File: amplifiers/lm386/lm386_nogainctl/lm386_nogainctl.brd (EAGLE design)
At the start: 55.5 x 35.3 mm, 12 parts, among them IC1 LM386N-4

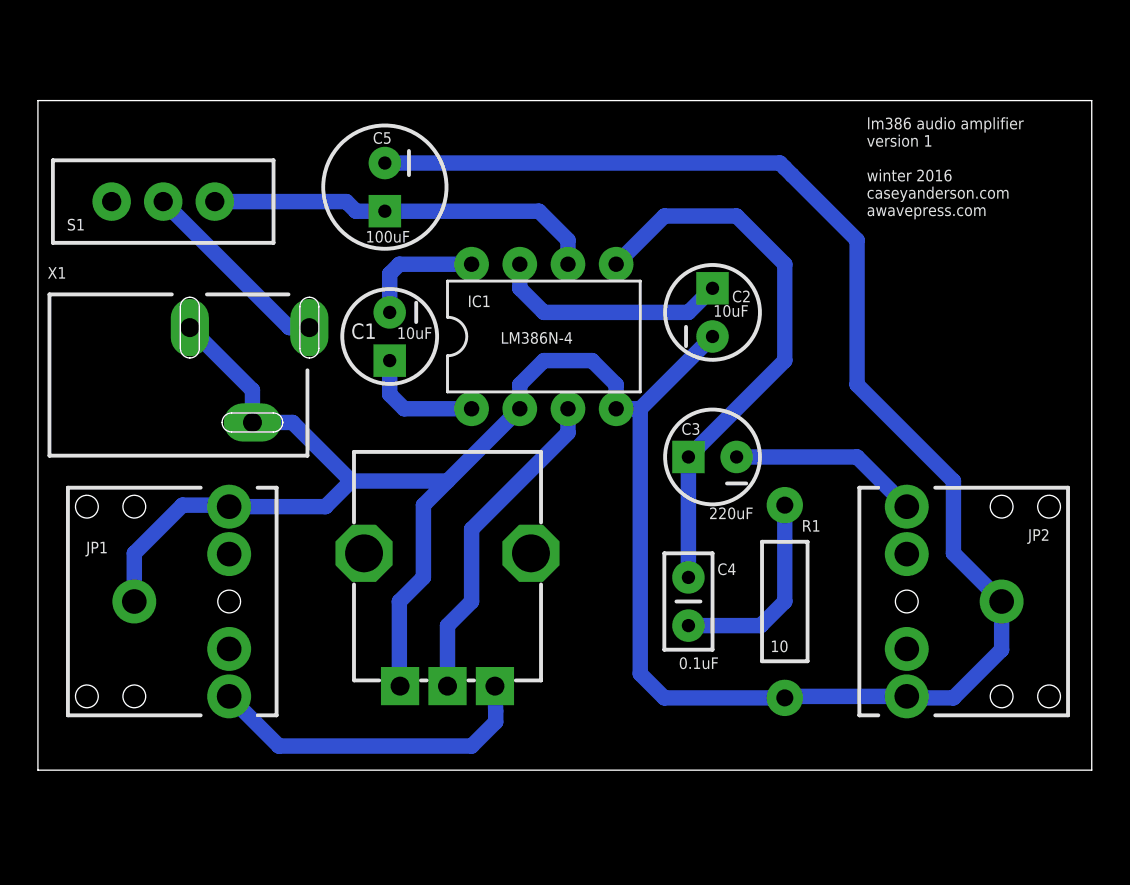
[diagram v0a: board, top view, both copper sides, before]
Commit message: updated to version 3, check on screw size and hole placement needed for confirmation
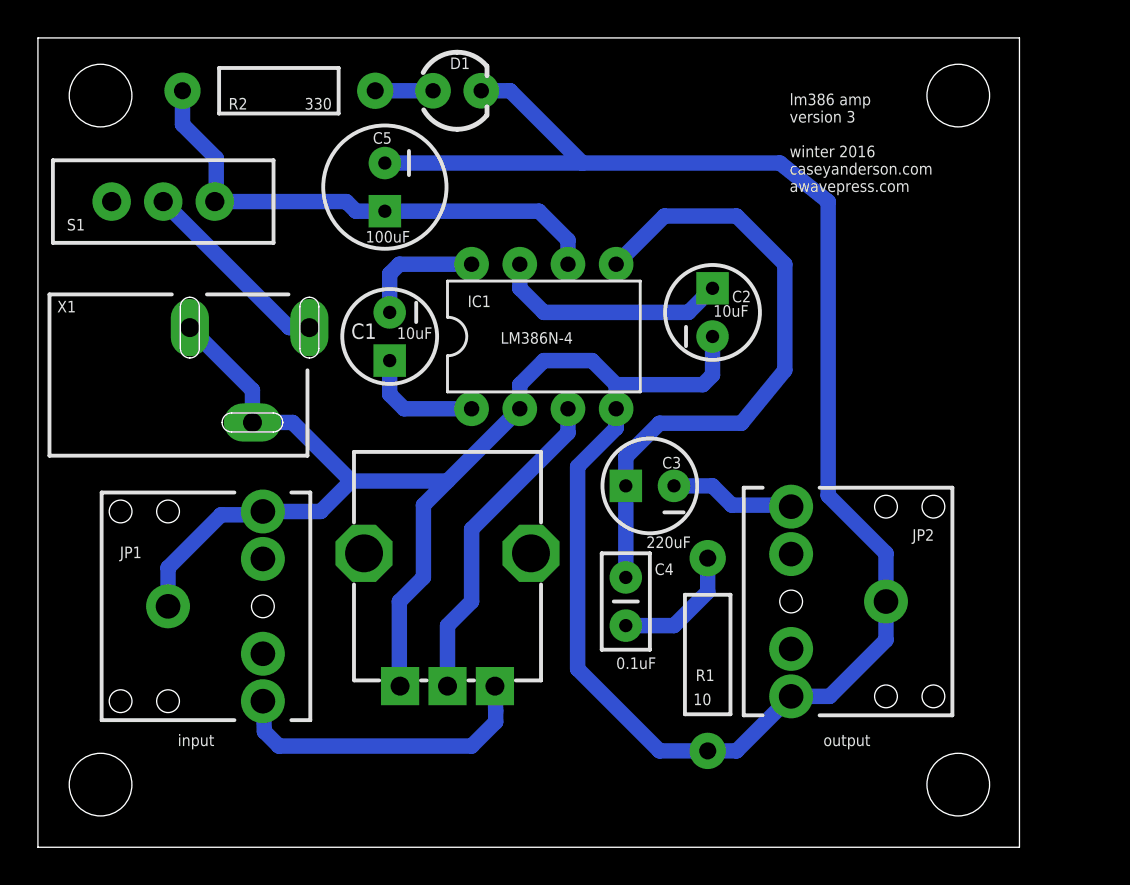
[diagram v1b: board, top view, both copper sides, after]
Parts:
- added D1: (no value), SparkFun-LED:LED3MM
- added R2: 330, SparkFun-Resistors:AXIAL-0.4
- added U$1, U$2, U$3, U$4: (no value), SparkFun-Electromechanical:STAND-OFF
- moved JP2 6.10 mm to (44.7, 8.89)
- moved R1 4.93 mm to (35.3, 6.10)
- moved C3 3.64 mm to (32.3, 15.0)
- moved C4 3.30 mm to (31.0, 10.2)
- moved JP1 1.80 mm to (6.86, 8.64)
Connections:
- new net N$10: D1.A, R2.P$1
- net GND: now also D1.K
- net N$4: now also R2.P$2
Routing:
- net N$4: track 20.7 -> 27.3 mm
- net N$9: track 10.7 -> 6.83 mm
- net N$8: track 29.6 -> 33.4 mm
- net GND: track 152.2 -> 155.7 mm
- net N$11: track 10.1 -> 6.63 mm
- net N$10: track 0.00 -> 3.05 mm
- net N$1: track 17.6 -> 16.5 mm
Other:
- board size 55.5 x 35.3 mm -> 51.7 x 42.7 mm
- board text added: "input"
- board text added: "lm386 amp version 3 winter 2016 caseyanderson.com awavepress.com"
- board text added: "output"
- board text removed: "lm386 audio amplifier version 1 winter 2016 caseyanderson.com awavepress.com"

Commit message: most recent lm386_nogainctl added
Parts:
- moved JP1 2.30 mm to (7.11, 10.9)
- moved U$3 2.29 mm to (48.5, 1.52)
- moved U$4 2.29 mm to (3.30, 1.52)
- moved JP2 2.03 mm to (44.7, 10.9)
- moved C3 1.83 mm to (33.8, 16.0)
- moved X1 1.80 mm to (0.76, 22.6)
- moved C4 1.52 mm to (31.0, 11.7)
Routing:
- net GND: track 155.7 -> 151.9 mm
- net N$8: track 33.4 -> 30.9 mm
- net N$11: track 6.63 -> 4.69 mm
- net N$9: track 6.83 -> 5.16 mm
- net N$1: track 16.5 -> 17.8 mm
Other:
- board size 51.7 x 42.7 mm -> 51.7 x 40.4 mm

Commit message: spacing update (just guessing)
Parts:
- moved X1 0.51 mm to (0.76, 22.1)
- moved S1 0.36 mm to (6.86, 30.2)
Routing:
- net GND: track 151.9 -> 153.0 mm
- net N$3: track 10.6 -> 11.2 mm
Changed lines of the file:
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@@
 <?xml version="1.0" encoding="utf-8"?>
 <!DOCTYPE eagle SYSTEM "eagle.dtd">
-<eagle version="7.4.0">
+<eagle version="8.7.0">
 <drawing>
 <settings>
 <setting alwaysvectorfont="no"/>
+<setting keepoldvectorfont="yes"/>
 <setting verticaltext="up"/>
 </settings>
@@
 <param name="dpMaxLengthDifference" value="10mm"/>
 <param name="dpGapFactor" value="2.5"/>
-<param name="checkGrid" value="0"/>
 <param name="checkAngle" value="0"/>
 <param name="checkFont" value="1"/>
 <param name="checkRestrict" value="1"/>
+<param name="checkStop" value="0"/>
+<param name="checkValues" value="0"/>
 <param name="useDiameter" value="13"/>
 <param name="maxErrors" value="50"/>
@@
 </element>
 <element name="C5" library="SparkFun-Capacitors" package="CPOL-RADIAL-100UF-25V" value="100uF" x="18.288" y="30.734" smashed="yes" rot="R270">
+<attribute name="NAME" x="17.653" y="33.02" size="0.6096" layer="25" font="vector" ratio="15"/>
 <attribute name="PROD_ID" value="CAP-08439" x="18.288" y="30.734" size="1.778" layer="27" rot="R270" display="off"/>
 <attribute name="VALUE" x="17.272" y="27.813" size="0.6096" layer="21" font="vector" ratio="15"/>
-<attribute name="NAME" x="17.653" y="33.02" size="0.6096" layer="25" font="vector" ratio="15"/>
-</element>
-<element name="S1" library="SparkFun-Electromechanical" package="SWITCH-SPDT_LOCK.007S" value="" x="6.604" y="29.972" smashed="yes" rot="R270">
-<attribute name="NAME" x="1.524" y="28.448" size="0.6096" layer="25" font="vector" ratio="15"/>
-<attribute name="VALUE" x="-2.921" y="33.782" size="1.778" layer="27" ratio="10" rot="R270"/>
+</element>
+<element name="S1" library="SparkFun-Electromechanical" package="SWITCH-SPDT_LOCK.007S" value="" x="6.858" y="30.226" smashed="yes" rot="R270">
+<attribute name="NAME" x="1.778" y="28.702" size="0.6096" layer="25" font="vector" ratio="15"/>
+<attribute name="VALUE" x="-2.667" y="34.036" size="1.778" layer="27" ratio="10" rot="R270"/>
 </element>
 <element name="C4" library="SparkFun-Capacitors" package="CAP-PTH-SMALL2" value="0.1uF" x="30.988" y="11.684" smashed="yes" rot="R270">
@@
 <attribute name="VALUE" x="30.48" y="6.858" size="0.6096" layer="21" font="vector" ratio="15"/>
 </element>
-<element name="X1" library="con-shiua-chyuan" package="SCD-014-A" value="" x="0.762" y="22.606" smashed="yes" rot="R270">
-<attribute name="OC_FARNELL" value="unknown" x="0.762" y="22.606" size="1.778" layer="27" rot="R270" display="off"/>
-<attribute name="MPN" value="" x="0.762" y="22.606" size="1.778" layer="27" rot="R270" display="off"/>
-<attribute name="OC_NEWARK" value="unknown" x="0.762" y="22.606" size="1.778" layer="27" rot="R270" display="off"/>
-<attribute name="MF" value="" x="0.762" y="22.606" size="1.778" layer="27" rot="R270" display="off"/>
-<attribute name="NAME" x="1.27" y="25.908" size="0.6096" layer="25" font="vector" ratio="15"/>
-<attribute name="VALUE" x="0.762" y="16.256" size="1.778" layer="27"/>
+<element name="X1" library="con-shiua-chyuan" package="SCD-014-A" value="" x="0.762" y="22.098" smashed="yes" rot="R270">
+<attribute name="MF" value="" x="0.762" y="22.098" size="1.778" layer="27" rot="R270" display="off"/>
+<attribute name="MPN" value="" x="0.762" y="22.098" size="1.778" layer="27" rot="R270" display="off"/>
+<attribute name="NAME" x="1.27" y="25.4" size="0.6096" layer="25" font="vector" ratio="15"/>
+<attribute name="OC_FARNELL" value="unknown" x="0.762" y="22.098" size="1.778" layer="27" rot="R270" display="off"/>
+<attribute name="OC_NEWARK" value="unknown" x="0.762" y="22.098" size="1.778" layer="27" rot="R270" display="off"/>
+<attribute name="VALUE" x="0.762" y="15.748" size="1.778" layer="27"/>
 </element>
 <element name="U$1" library="SparkFun-Electromechanical" package="STAND-OFF" value="" x="3.302" y="35.56"/>
@@
 <wire x1="23.368" y1="35.814" x2="24.892" y2="35.814" width="0.8128" layer="16"/>
 <wire x1="24.892" y1="35.814" x2="28.702" y2="32.004" width="0.8128" layer="16"/>
-<wire x1="8.262" y1="25.106" x2="8.262" y2="23.406" width="0.8128" layer="16"/>
-<wire x1="8.262" y1="23.406" x2="11.562" y2="20.106" width="0.8128" layer="16"/>
-<wire x1="11.562" y1="20.106" x2="11.562" y2="16.472" width="0.8128" layer="16"/>
-<wire x1="11.562" y1="16.472" x2="12.112" y2="15.922" width="0.8128" layer="16"/>
 <wire x1="12.112" y1="15.922" x2="15.066" y2="15.922" width="0.8128" layer="16"/>
 <wire x1="15.066" y1="15.922" x2="15.748" y2="15.24" width="0.8128" layer="16"/>
@@
 <wire x1="30.48" y1="20.32" x2="33.02" y2="20.32" width="0.8128" layer="16"/>
 <wire x1="33.02" y1="20.32" x2="35.56" y2="22.86" width="0.8128" layer="16"/>
+<wire x1="12.112" y1="15.922" x2="11.562" y2="16.472" width="0.8128" layer="16"/>
+<wire x1="11.562" y1="16.472" x2="11.562" y2="19.598" width="0.8128" layer="16"/>
+<wire x1="11.562" y1="19.598" x2="11.562" y2="23.998" width="0.8128" layer="16"/>
+<wire x1="11.562" y1="23.998" x2="10.922" y2="24.638" width="0.8128" layer="16"/>
+<wire x1="10.922" y1="24.638" x2="8.302" y2="24.638" width="0.8128" layer="16"/>
+<wire x1="8.302" y1="24.638" x2="8.262" y2="24.598" width="0.8128" layer="16"/>
 </signal>
 <signal name="N$4">
@@
 <wire x1="26.416" y1="29.464" x2="27.94" y2="27.94" width="0.8128" layer="16"/>
 <wire x1="27.94" y1="27.94" x2="27.94" y2="26.67" width="0.8128" layer="16"/>
-<wire x1="9.398" y1="29.972" x2="16.256" y2="29.972" width="0.8128" layer="16"/>
-<wire x1="16.256" y1="29.972" x2="16.764" y2="29.464" width="0.8128" layer="16"/>
-<wire x1="16.764" y1="29.464" x2="18.288" y2="29.464" width="0.8128" layer="16"/>
 <wire x1="18.288" y1="29.464" x2="26.416" y2="29.464" width="0.8128" layer="16"/>
 <contactref element="R2" pad="P$2"/>
-<wire x1="9.3218" y1="29.972" x2="9.398" y2="29.972" width="0.8128" layer="16"/>
-<wire x1="9.398" y1="29.972" x2="9.398" y2="32.258" width="0.8128" layer="16"/>
-<wire x1="9.398" y1="32.258" x2="7.62" y2="34.036" width="0.8128" layer="16"/>
-<wire x1="7.62" y1="34.036" x2="7.62" y2="35.814" width="0.8128" layer="16"/>
+<wire x1="9.5758" y1="30.226" x2="9.5758" y2="33.6042" width="0.8128" layer="16"/>
+<wire x1="7.62" y1="35.56" x2="7.62" y2="35.814" width="0.8128" layer="16"/>
+<wire x1="9.5758" y1="33.6042" x2="7.62" y2="35.56" width="0.8128" layer="16"/>
+<wire x1="9.5758" y1="30.226" x2="10.3378" y2="29.464" width="0.8128" layer="16"/>
+<wire x1="10.3378" y1="29.464" x2="18.288" y2="29.464" width="0.8128" layer="16"/>
 </signal>
 <signal name="N$5">
@@
 <contactref element="S1" pad="2"/>
 <contactref element="X1" pad="1"/>
-<wire x1="14.562" y1="25.106" x2="12.232" y2="25.106" width="0.8128" layer="16"/>
-<wire x1="12.232" y1="25.106" x2="9.144" y2="27.94" width="0.8128" layer="16"/>
-<wire x1="9.144" y1="27.94" x2="7.366" y2="27.94" width="0.8128" layer="16"/>
-<wire x1="7.366" y1="27.94" x2="6.604" y2="28.956" width="0.8128" layer="16"/>
-<wire x1="6.604" y1="28.956" x2="6.604" y2="29.972" width="0.8128" layer="16"/>
+<wire x1="14.562" y1="24.598" x2="11.982" y2="27.178" width="0.8128" layer="16"/>
+<wire x1="7.874" y1="27.178" x2="6.858" y2="28.194" width="0.8128" layer="16"/>
+<wire x1="11.982" y1="27.178" x2="7.874" y2="27.178" width="0.8128" layer="16"/>
+<wire x1="6.858" y1="28.194" x2="6.858" y2="30.226" width="0.8128" layer="16"/>
 </signal>
 <signal name="N$10">
